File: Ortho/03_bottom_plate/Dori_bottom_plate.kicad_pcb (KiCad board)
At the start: 2 copper layers, 308 x 111.1 mm, 84 parts, among them J1 4PIN, J2 4PIN, U1 HOLE, U10 HOLE, U11 HOLE, U12 HOLE, U13 HOLE, U14 HOLE, U15 HOLE, U16 HOLE, U17 HOLE, U18 HOLE, U19 HOLE, U2 HOLE, U20 HOLE, U21 HOLE, U22 HOLE, U23 HOLE, U24 HOLE, U25 HOLE, U26 HOLE, U27 HOLE, U28 HOLE, U29 HOLE, U3 HOLE, U30 HOLE, U31 HOLE, U32 HOLE, U33 HOLE, U34 HOLE, U35 HOLE, U36 HOLE, U37 HOLE, U38 HOLE, U39 HOLE, U4 HOLE, U40 HOLE, U41 HOLE, U42 HOLE, U43 HOLE, U44 HOLE, U45 HOLE, U46 HOLE, U47 HOLE, U48 HOLE, U49 HOLE, U5 HOLE, U50 HOLE, U51 HOLE, U52 HOLE, U53 HOLE, U54 HOLE, U55 HOLE, U56 HOLE, U57 HOLE, U58 HOLE, U59 HOLE, U6 HOLE, U60 HOLE, U61 HOLE, U62 HOLE, U63 HOLE, U64 HOLE, U65 HOLE, U66 HOLE, U67 HOLE, U68 HOLE, U7 HOLE, U8 HOLE, U9 HOLE

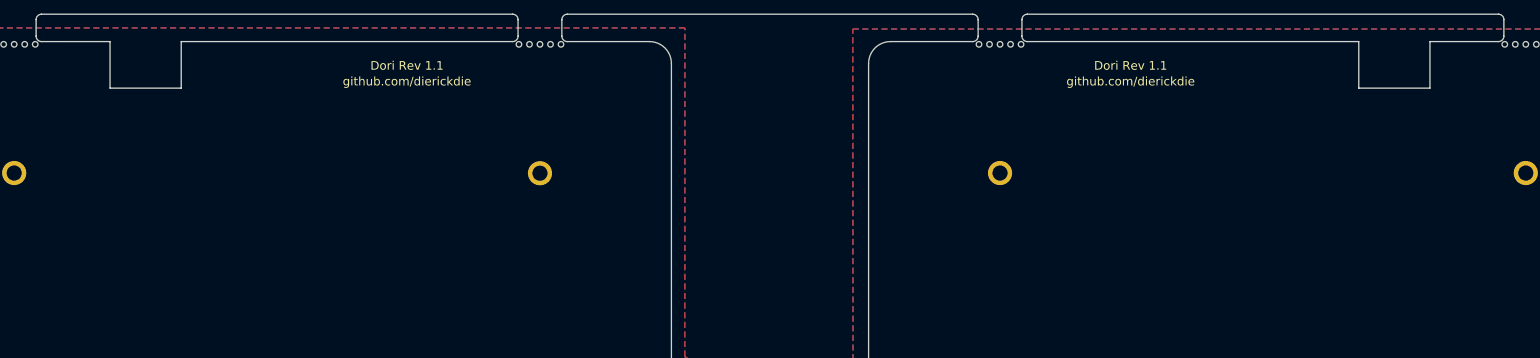
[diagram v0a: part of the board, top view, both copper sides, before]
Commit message: Moved USB port
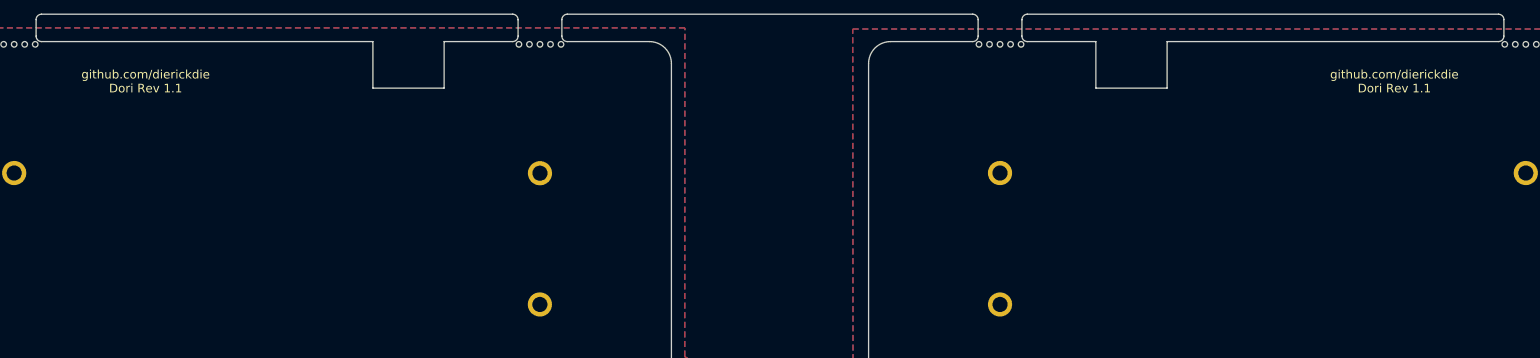
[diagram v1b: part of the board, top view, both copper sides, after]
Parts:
- added H13: MountingHole, random-keyboard-parts:Generic-Mounthole, F.Cu at (211.9, 81.0)
- added H14: MountingHole, random-keyboard-parts:Generic-Mounthole, F.Cu at (278.6, 81.0)
- moved U50 0.18 mm to (259.6, 116.7)
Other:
- outline, holes or cut-outs redrawn
- board text added: "github.com/dierickdie Dori Rev 1.1"
- board text removed: "Dori Rev 1.1"
- board text removed: "github.com/dierickdie"
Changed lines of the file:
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@@
-(kicad_pcb (version 20171130) (host pcbnew "(5.1.2-1)-1")
+(kicad_pcb (version 20171130) (host pcbnew "(5.1.4-0-10_14)")
   (general
     (thickness 1.6)
-    (drawings 197)
+    (drawings 195)
     (tracks 4)
     (zones 0)
-    (modules 84)
+    (modules 86)
     (nets 3)
   )
@@
     (uvia_drill 0.2)
   )
+  (module random-keyboard-parts:Generic-Mounthole (layer F.Cu)
+    (at 278.60625 80.9625)
+    (attr virtual)
+    (fp_text reference H14 (at 0 2) (layer Dwgs.User)
+      (effects (font (size 1 1) (thickness 0.15)))
+    )
+    (fp_text value MountingHole (at 0 -2) (layer Dwgs.User)
+      (effects (font (size 1 1) (thickness 0.15)))
+    )
+    (pad 1 thru_hole circle (at 0 0) (size 3.5 3.5) (drill 2.2) (layers *.Cu *.Mask))
+  )
+  (module random-keyboard-parts:Generic-Mounthole (layer F.Cu)
+    (at 211.91855 80.9625)
+    (attr virtual)
+    (fp_text reference H13 (at 0 2) (layer Dwgs.User)
+      (effects (font (size 1 1) (thickness 0.15)))
+    )
+    (fp_text value MountingHole (at 0 -2) (layer Dwgs.User)
+      (effects (font (size 1 1) (thickness 0.15)))
+    )
+    (pad 1 thru_hole circle (at 0 0) (size 3.5 3.5) (drill 2.2) (layers *.Cu *.Mask))
+  )
+  (module random-keyboard-parts:Generic-Mounthole locked (layer F.Cu)
+    (at 135.73125 61.9125)
+    (attr virtual)
+    (fp_text reference H1 (at 0 2) (layer Dwgs.User)
+      (effects (font (size 1 1) (thickness 0.15)))
+    )
+    (fp_text value MountingHole (at 0 -2) (layer Dwgs.User)
+      (effects (font (size 1 1) (thickness 0.15)))
+    )
+    (pad 1 thru_hole circle (at 0 0) (size 3.5 3.5) (drill 2.2) (layers *.Cu *.Mask))
+  )
   (module Keebio-Parts:TRRS-PJ-320A (layer F.Cu)
     (at 253.20625 95.25 30)
@@
   )
   (module Keeb_footprints:MX100_outline (layer F.Cu)
-    (at 259.55625 116.498801 30)
+    (at 259.55625 116.68125 30)
     (fp_text reference U50 (at 0.0254 3.1623 -150) (layer Cmts.User)
       (effects (font (size 1 1) (thickness 0.15) italic))
@@
   )
   (module random-keyboard-parts:Generic-Mounthole locked (layer F.Cu)
-    (at 135.73125 61.9125)
-    (attr virtual)
-    (fp_text reference H1 (at 0 2) (layer Dwgs.User)
-      (effects (font (size 1 1) (thickness 0.15)))
-    )
-    (fp_text value MountingHole (at 0 -2) (layer Dwgs.User)
-      (effects (font (size 1 1) (thickness 0.15)))
-    )
-    (pad 1 thru_hole circle (at 0 0) (size 3.5 3.5) (drill 2.2) (layers *.Cu *.Mask))
-  )
-  (module random-keyboard-parts:Generic-Mounthole locked (layer F.Cu)
     (at 211.93125 61.94)
     (attr virtual)
@@
     (pad 1 thru_hole circle (at 0 0) (size 3.5 3.5) (drill 2.2) (layers *.Cu *.Mask))
   )
+  (gr_line (start 198.040625 42.8625) (end 207.9625 42.8625) (layer Edge.Cuts) (width 0.05))
+  (gr_line (start 139.7 42.8625) (end 187.721875 42.860734) (layer Edge.Cuts) (width 0.05))
+  (gr_line (start 292.496875 42.8625) (end 282.575 42.8625) (layer Edge.Cuts) (width 0.05))
+  (gr_line (start 350.8375 42.8625) (end 302.815625 42.8625) (layer Edge.Cuts) (width 0.05))
   (gr_arc (start 233.870499 127.254001) (end 233.1085 128.651) (angle -81.74056202) (layer Edge.Cuts) (width 0.05))
   (gr_line (start 243.1415 114.3) (end 235.143543 128.208783) (layer Edge.Cuts) (width 0.05))
@@
   )
   (gr_line (start 200.025 119.060306) (end 197.64375 119.0625) (layer Edge.Cuts) (width 0.05))
-  (gr_line (start 330.596875 49.609375) (end 340.915625 49.609375) (layer Edge.Cuts) (width 0.05))
-  (gr_line (start 340.915625 49.609375) (end 340.915625 42.8625) (layer Edge.Cuts) (width 0.05))
-  (gr_line (start 330.596875 42.8625) (end 330.596875 49.609375) (layer Edge.Cuts) (width 0.05))
-  (gr_line (start 159.940625 49.609375) (end 159.940625 42.8625) (layer Edge.Cuts) (width 0.05))
-  (gr_line (start 149.621875 49.609375) (end 159.940625 49.609375) (layer Edge.Cuts) (width 0.05))
-  (gr_line (start 149.621875 42.860734) (end 149.621875 49.609375) (layer Edge.Cuts) (width 0.05))
-  (gr_line (start 139.7 42.8625) (end 149.621875 42.860734) (layer Edge.Cuts) (width 0.05))
+  (gr_line (start 292.496875 49.609375) (end 302.815625 49.609375) (layer Edge.Cuts) (width 0.05))
+  (gr_line (start 302.815625 49.609375) (end 302.815625 42.8625) (layer Edge.Cuts) (width 0.05))
+  (gr_line (start 292.496875 42.8625) (end 292.496875 49.609375) (layer Edge.Cuts) (width 0.05))
+  (gr_line (start 198.040625 49.609375) (end 198.040625 42.8625) (layer Edge.Cuts) (width 0.05))
+  (gr_line (start 187.721875 49.609375) (end 198.040625 49.609375) (layer Edge.Cuts) (width 0.05))
+  (gr_line (start 187.721875 42.860734) (end 187.721875 49.609375) (layer Edge.Cuts) (width 0.05))
   (gr_line (start 374.65 64.690625) (end 374.65 65.484375) (layer B.SilkS) (width 0.25))
   (gr_line (start 374.65 63.103125) (end 374.65 63.896875) (layer B.SilkS) (width 0.25))
@@
     (arrow2b (pts (xy 85.995 141.2875) (xy 85.408579 140.160996)))
   )
-  (gr_text "Dori Rev 1.1" (at 192.66 46.36) (layer F.SilkS)
-    (effects (font (size 1.25 1.25) (thickness 0.2)))
-  )
-  (gr_text github.com/dierickdie (at 192.659244 48.64) (layer F.SilkS)
+  (gr_text "github.com/dierickdie\nDori Rev 1.1" (at 154.78125 48.64) (layer F.SilkS)
     (effects (font (size 1.25 1.25) (thickness 0.2)))
   )
@@
     (arrow2b (pts (xy 110.33125 34.147548) (xy 111.457754 33.561127)))
   )
-  (gr_line (start 207.9625 42.8625) (end 159.940625 42.8625) (layer Edge.Cuts) (width 0.05))
   (gr_line (start 227.80625 42.8625) (end 215.9 42.8625) (layer Edge.Cuts) (width 0.05))
   (gr_line (start 131.7625 42.8625) (end 119.85625 42.8625) (layer Edge.Cuts) (width 0.05))
@@
   (gr_line (start 282.575 38.89375) (end 350.8375 38.89375) (layer Edge.Cuts) (width 0.05))
   (gr_line (start 358.775 42.8625) (end 370.68125 42.8625) (layer Edge.Cuts) (width 0.05))
-  (gr_line (start 350.8375 42.8625) (end 340.915625 42.8625) (layer Edge.Cuts) (width 0.05))
-  (gr_line (start 282.575 42.8625) (end 330.596875 42.8625) (layer Edge.Cuts) (width 0.05))
   (gr_line (start 281.78125 39.6875) (end 281.78125 42.06875) (layer Edge.Cuts) (width 0.05))
   (gr_line (start 274.6375 42.8625) (end 262.73125 42.8625) (layer Edge.Cuts) (width 0.05))
@@
   (gr_line (start 115.094464 66.421) (end 115.09375 95.504) (layer Edge.Cuts) (width 0.05))
   (gr_line (start 116.68125 66.421) (end 116.680536 95.504) (layer Edge.Cuts) (width 0.05))
-  (gr_text github.com/dierickdie (at 297.539244 48.64) (layer F.SilkS)
+  (gr_text "github.com/dierickdie\nDori Rev 1.1" (at 335.75625 48.64) (layer F.SilkS)
     (effects (font (size 1.25 1.25) (thickness 0.2)))
   )
   (gr_line (start 111.91875 119.0625) (end 94.45625 119.0625) (layer Edge.Cuts) (width 0.05))
-  (gr_text "Dori Rev 1.1" (at 297.54 46.36) (layer F.SilkS)
-    (effects (font (size 1.25 1.25) (thickness 0.2)))
-  )
   (gr_line (start 115.09375 115.8875) (end 115.094107 104.521) (layer Edge.Cuts) (width 0.05))
   (gr_line (start 116.68125 46.0375) (end 116.679822 57.261125) (layer Edge.Cuts) (width 0.05))
